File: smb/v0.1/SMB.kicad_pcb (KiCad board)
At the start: 2 copper layers, 100 x 86 mm, 91 parts, among them IC1 MAX485, IC101 ATMEGA1284-A, J101 RJ45, J102 RTS_RESET, J103 ICSP, J104 SERIAL_REV, J202 USD_CONN, J401 HR911105_RJ45, P1 CONN_2, P101 I2C_CONN, P102 CONN_3X2, P103 CONN_3X2, P104 CONN_3X2, P105 CONN_5, P106 CONN_3X2, P107 CONN_3, P108 CONN_5, P301 CONN_2, SW101 SKQGAKE010, U201 ENC28J60, U202 LM1117IMP-3.3, U301 74HC08, U302 MP2562DS, U303 74HC08, X101 20MHz, X201 25MHz

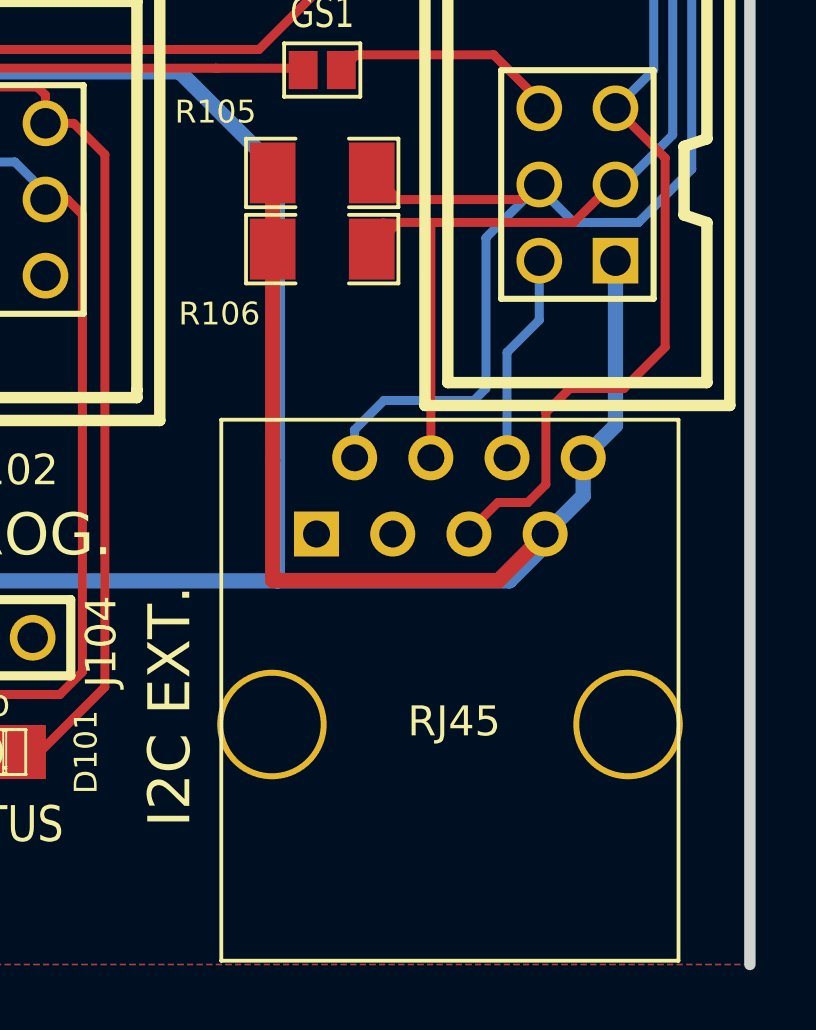
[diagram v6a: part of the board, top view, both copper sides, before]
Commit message: correction RJ45 du port I2C
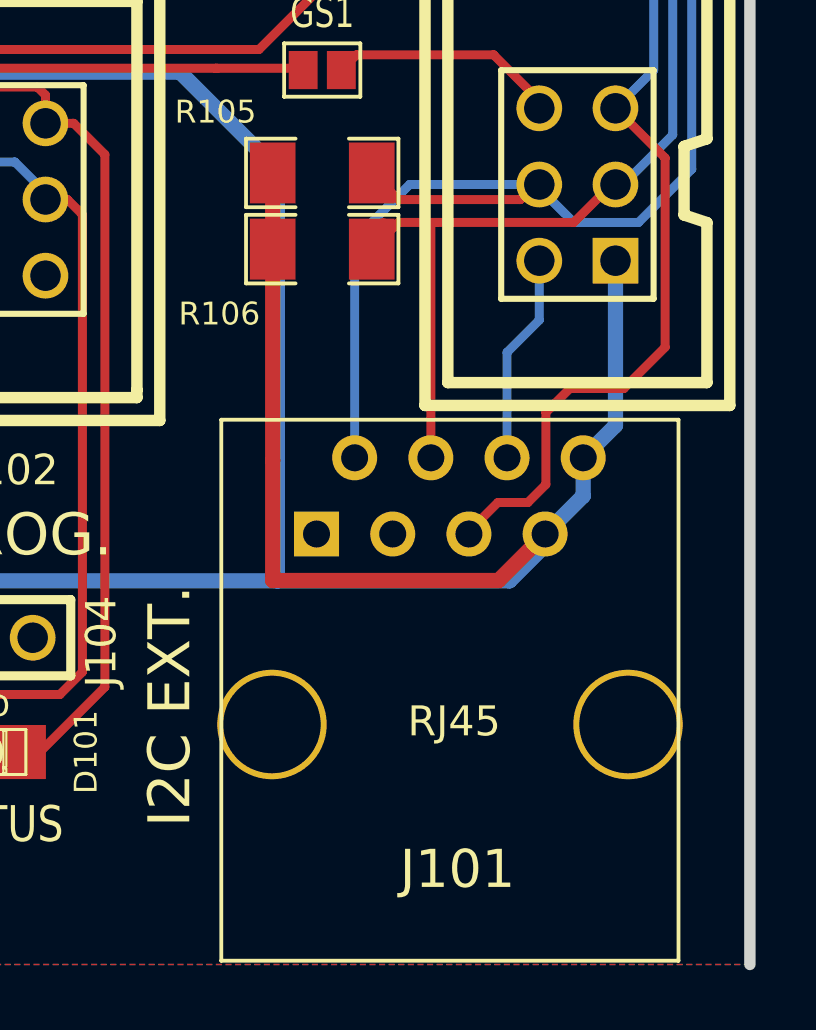
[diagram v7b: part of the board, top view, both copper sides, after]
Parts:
- J101: footprint RJ45_8 -> RJ45_BASIC
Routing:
- net SDA: track 101.9 -> 102.6 mm

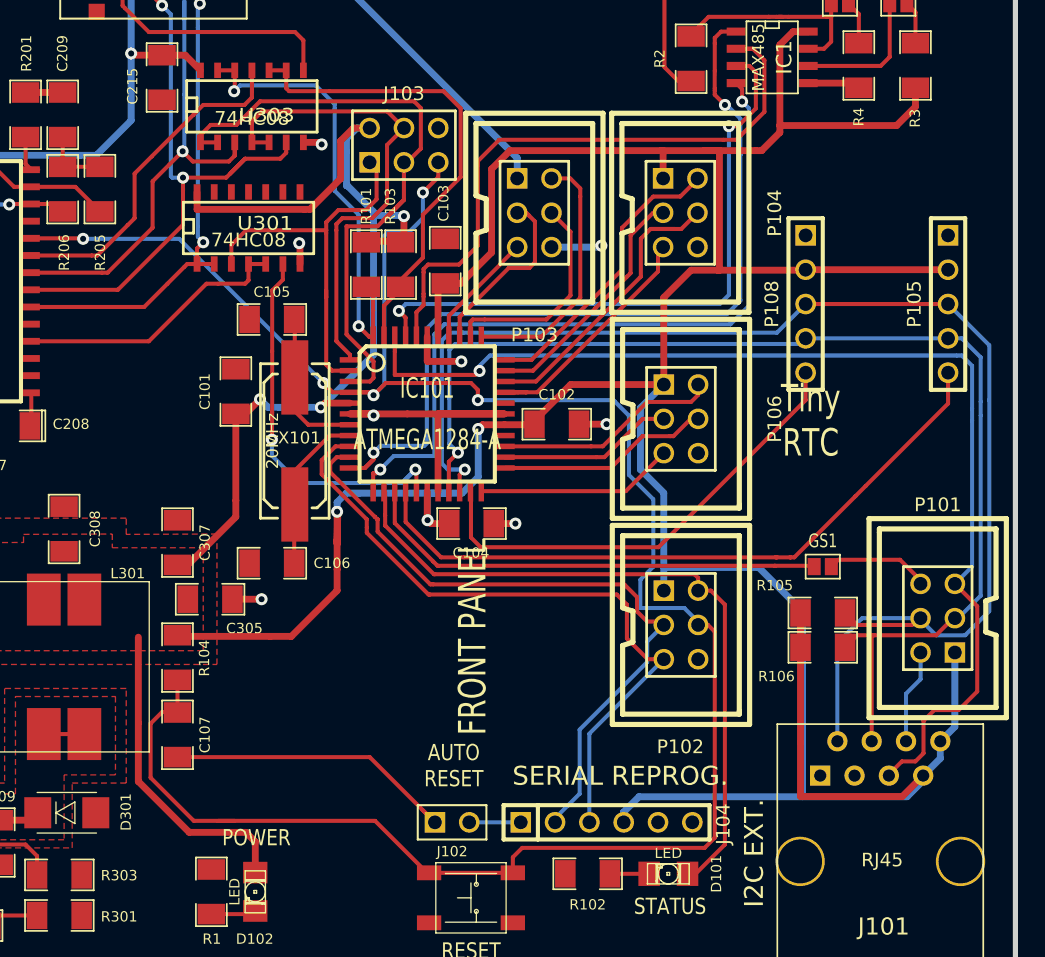
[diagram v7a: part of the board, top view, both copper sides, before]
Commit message: correction cablage RJ45 i2c pour etre conforme aux autres cartes 8in8out deplacement de connecteur pour liberer de la place pour les slots
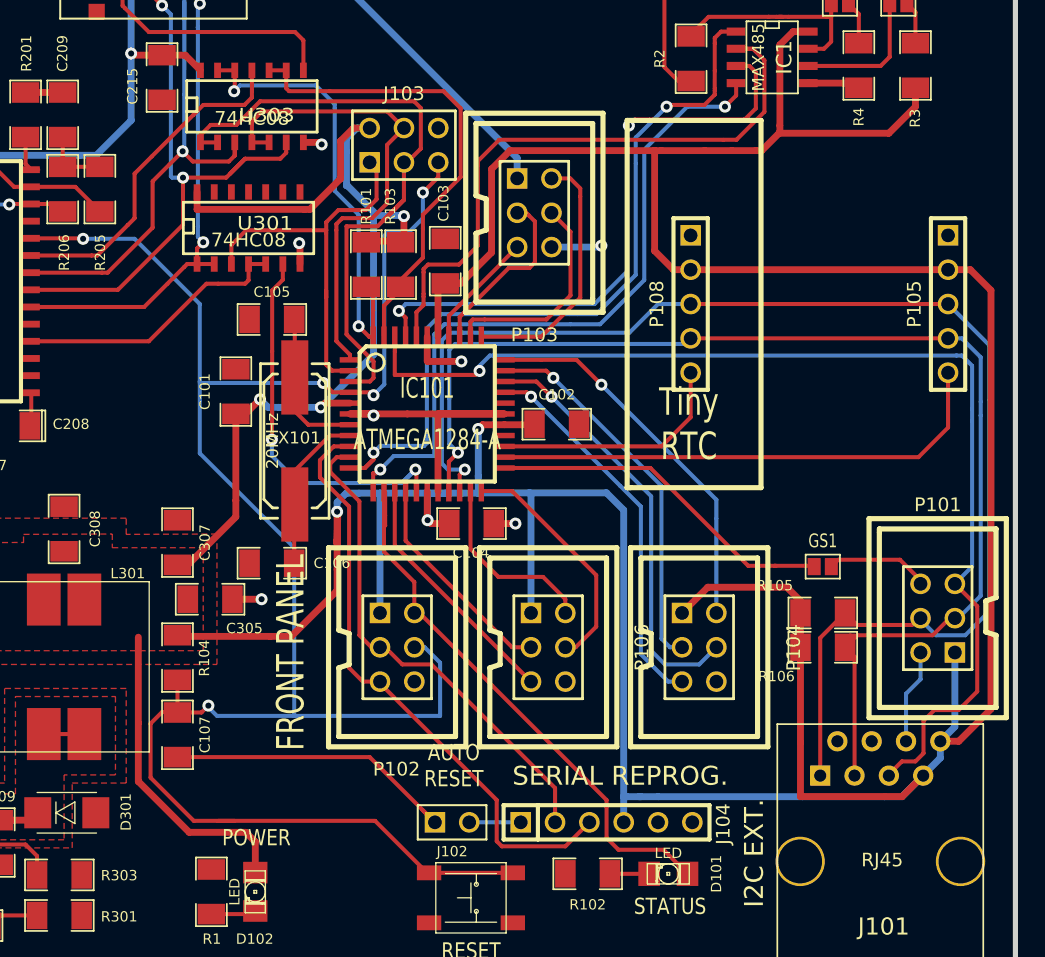
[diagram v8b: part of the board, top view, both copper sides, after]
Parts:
- moved P104 32.2 mm to (109.6, 89.2)
- moved P102 21.1 mm to (87.2, 89.2)
- moved P106 19.6 mm to (98.4, 89.2)
- moved P108 8.51 mm to (109.0, 63.8)
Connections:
- GS1 pad 2: N-0000010 -> N-000008
- IC101 pad 14: N-0000010 -> PD5
- IC101 pad 15: DS -> PD6
- IC101 pad 23: PC4 -> N-000008
- IC101 pad 25: PC6 -> DS
- J101 pad 1: GND -> SDA
- J101 pad 2: SDA -> GND
- J101 pad 3: GND -> SCL
- J101 pad 4: SCL -> GND
- P105 pad 5: DS -> PC5
- P106 pad 2: PC6 -> PC2
- P106 pad 3: PC5 -> PD6
- P106 pad 4: PC4 -> PC3
- P106 pad 5: PC3 -> PD5
- P108 pad 5: PC2 -> DS
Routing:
- net +5V: track 378.5 -> 418.1 mm
- net N-0000010: track 34.8 -> 0.00 mm
- net DS: track 50.6 -> 18.0 mm
- net N-000008: track 0.00 -> 26.0 mm
- net PC5: track 13.0 -> 37.8 mm
- net PC2: track 35.0 -> 13.9 mm
- net /RESET: track 166.6 -> 148.0 mm
- net PD5: track 0.00 -> 18.3 mm
- net PC6: track 16.7 -> 0.00 mm
- net PD6: track 0.00 -> 16.2 mm
- net PC4: track 15.9 -> 0.00 mm
- net TX0: track 50.8 -> 37.0 mm
- net PA5: track 18.2 -> 28.2 mm, vias 0 -> 1
- net LED_STATUS: track 52.1 -> 42.4 mm
- net PA7: track 18.7 -> 28.4 mm, vias 0 -> 1
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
